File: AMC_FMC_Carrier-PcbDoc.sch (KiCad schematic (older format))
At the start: 19 parts

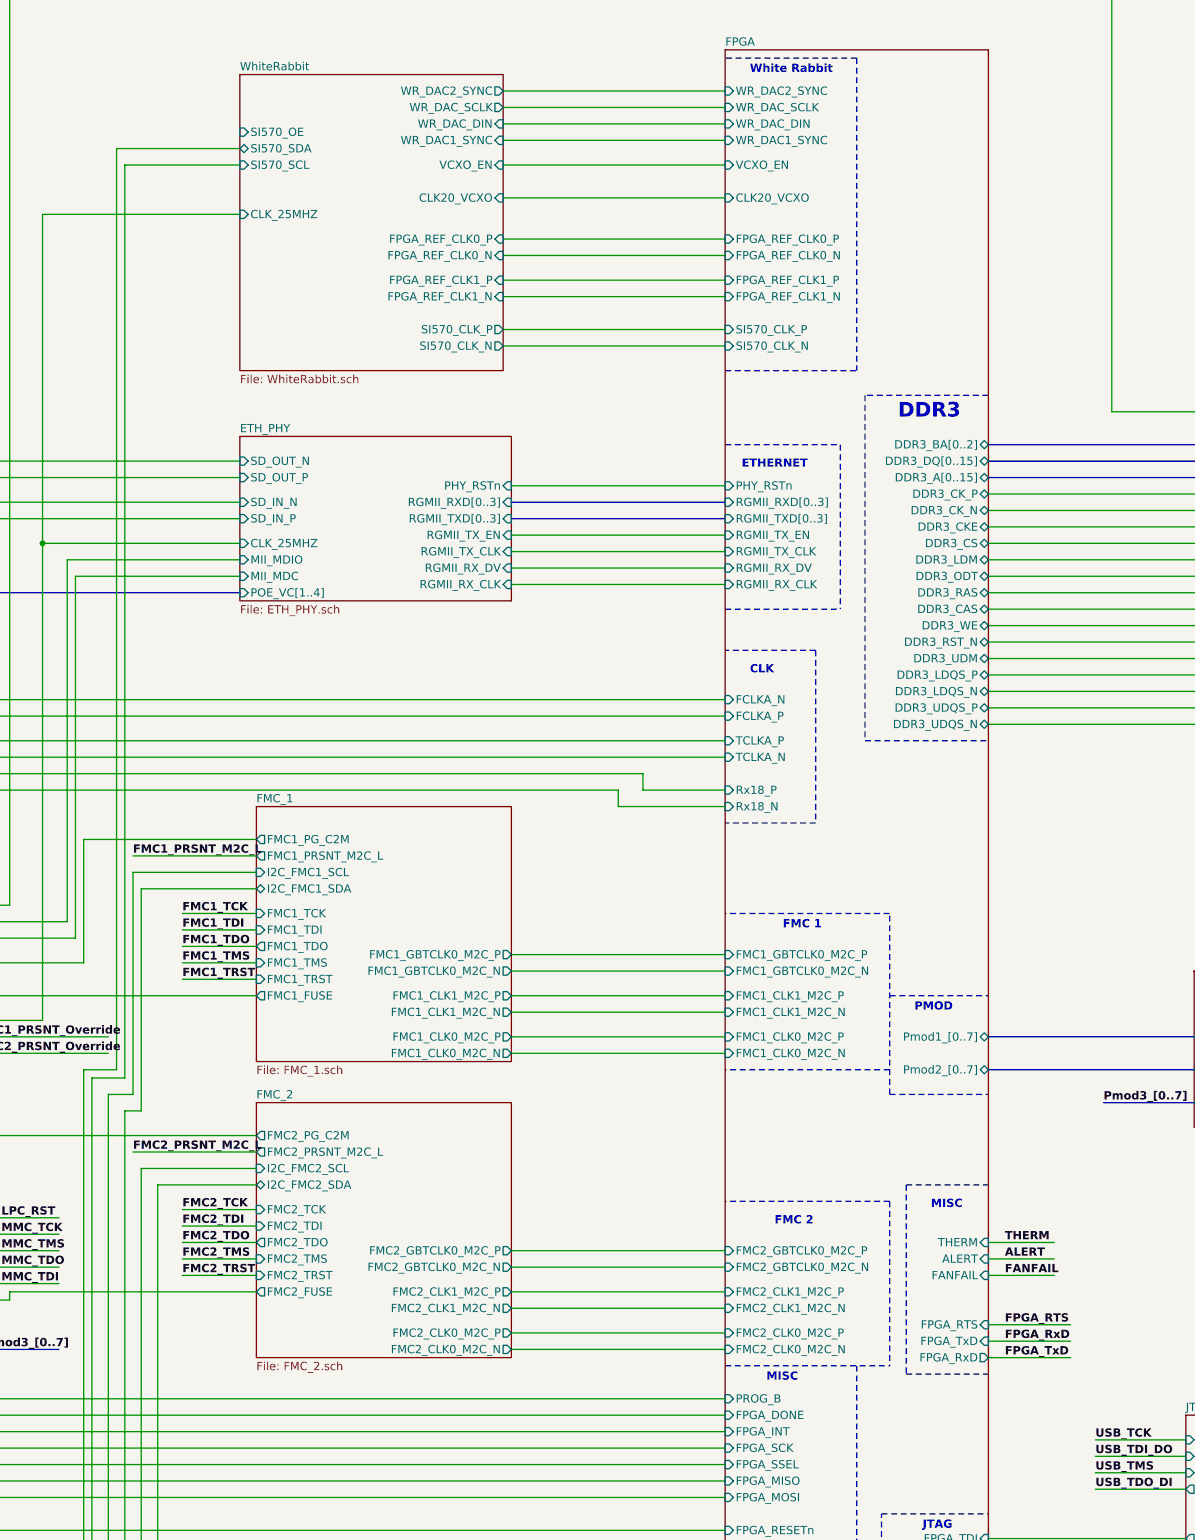
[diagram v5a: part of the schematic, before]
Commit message: SCH: connect SI570_OE to U39 P0_0 (pin 1)
... also rotated 6 net labels to make the
little _not connected_ square disappear
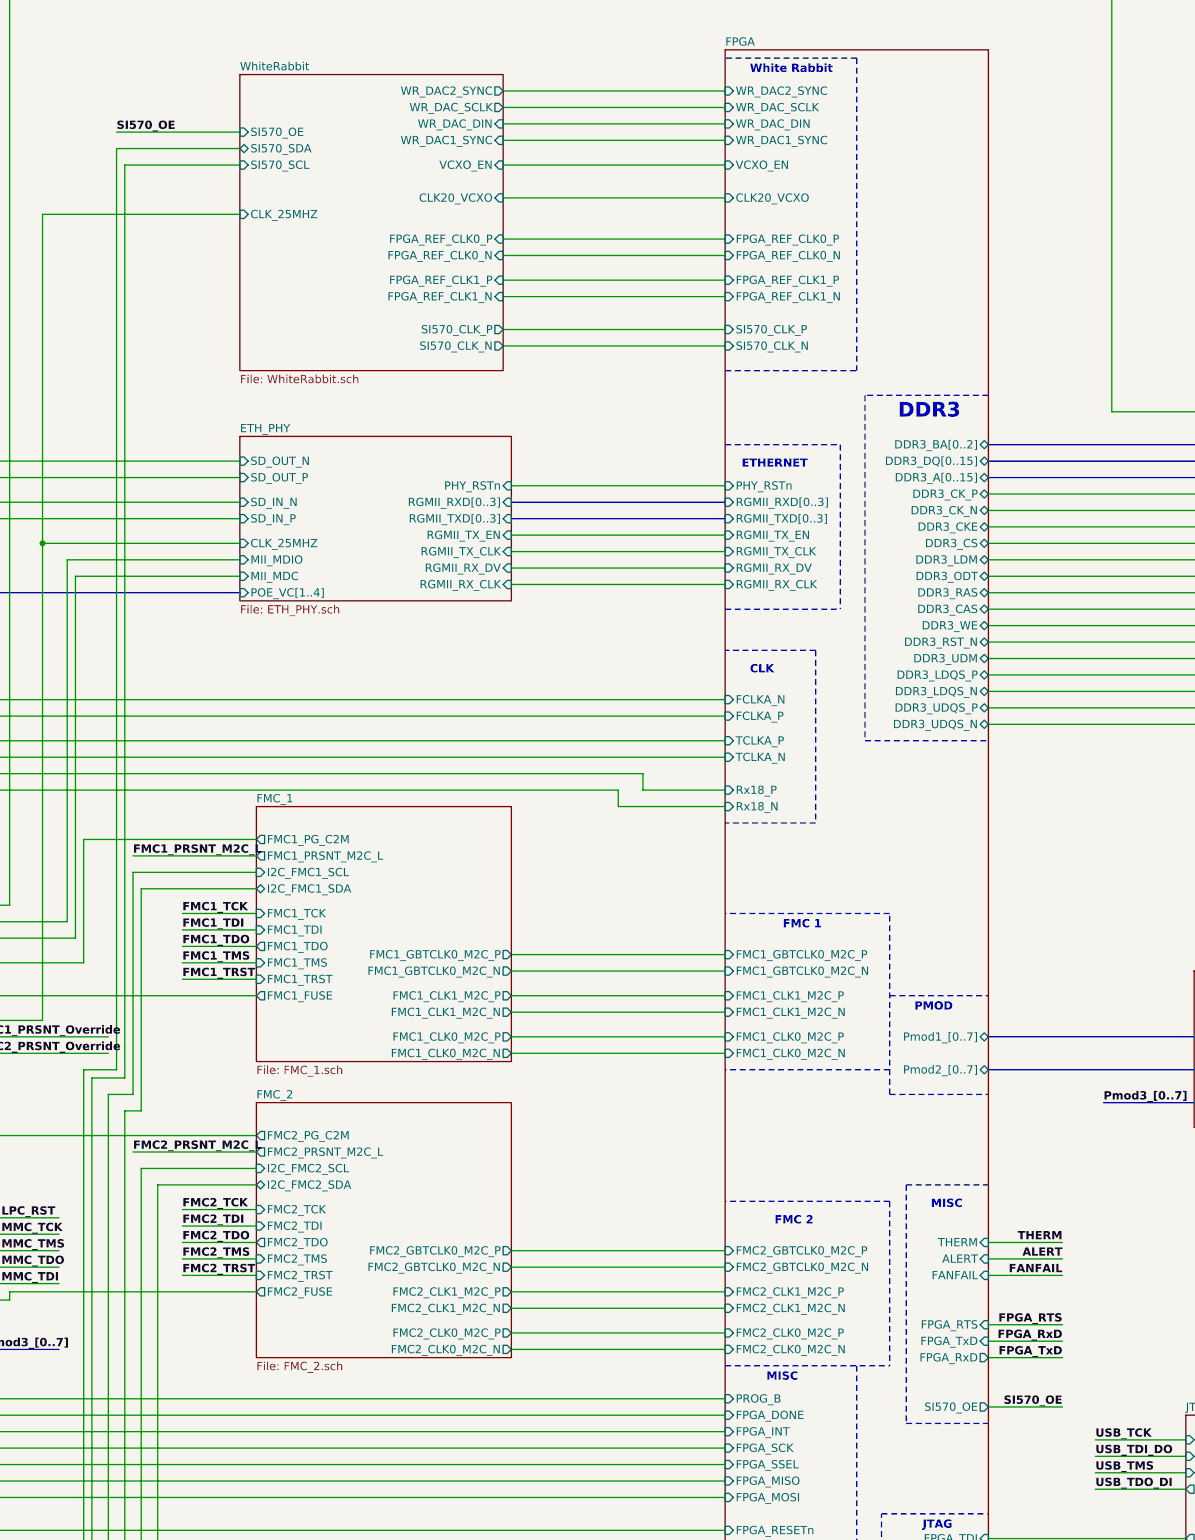
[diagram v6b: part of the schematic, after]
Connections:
- net labels added: SI570_OE
- wire segments 380 -> 382
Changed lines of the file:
@@
 F128 "SI570_CLK_P" I L 11350 3250 50
 F129 "SI570_CLK_N" I L 11350 3350 50
+F130 "SI570_OE" O R 12950 9800 50
 $EndSheet
 Wire Wire Line
@@
 Wire Wire Line
 	3500 10200 3100 10200
-Text Label 13050 8800 0    50   ~ 10
+Text Label 13400 8800 2    50   ~ 10
 THERM
-Text Label 13050 8900 0    50   ~ 10
+Text Label 13400 8900 2    50   ~ 10
 ALERT
-Text Label 13050 9000 0    50   ~ 10
+Text Label 13400 9000 2    50   ~ 10
 FANFAIL
 Wire Wire Line
-	13350 8800 12950 8800
-Wire Wire Line
-	13350 8900 12950 8900
-Wire Wire Line
-	13350 9000 12950 9000
+	13400 8800 12950 8800
+Wire Wire Line
+	13400 8900 12950 8900
+Wire Wire Line
+	13400 9000 12950 9000
 Wire Wire Line
 	6800 9750 11350 9750
@@
 Wire Bus Line
 	13650 7950 14200 7950
-Text Label 13050 9300 0    50   ~ 10
+Text Label 13400 9300 2    50   ~ 10
 FPGA_RTS
-Text Label 13050 9400 0    50   ~ 10
+Text Label 13400 9400 2    50   ~ 10
 FPGA_RxD
-Text Label 13050 9500 0    50   ~ 10
+Text Label 13400 9500 2    50   ~ 10
 FPGA_TxD
 Wire Wire Line
-	13450 9300 12950 9300
-Wire Wire Line
-	13450 9400 12950 9400
-Wire Wire Line
-	13450 9500 12950 9500
+	13400 9300 12950 9300
+Wire Wire Line
+	13400 9400 12950 9400
+Wire Wire Line
+	13400 9500 12950 9500
 Text Label 3550 8700 0    50   ~ 10
 FPGA_RTS
@@
 	12350 8550 12350 9550
 Wire Notes Line
-	12450 8450 12450 9600
-Wire Notes Line
-	12450 9600 12950 9600
+	12450 8450 12450 9900
+Wire Notes Line
+	12450 9900 12950 9900
 Wire Notes Line
 	12450 8450 12950 8450
@@
 Wire Wire Line
 	7450 7750 7650 7750
+Text Label 7650 2050 0    50   ~ 10
+SI570_OE
+Wire Wire Line
+	7650 2050 8400 2050
+Text Label 13400 9800 2    50   ~ 10
+SI570_OE
+Wire Wire Line
+	12950 9800 13400 9800
 $EndSCHEMATC

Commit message: Mounting holes
Add B13 near front panel
Un-ground B9 and B10, AMC features
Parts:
- added B13: PLATED_HOLE2.7_PAD5.0, Marble:HOLE2.7_PAD5.0, symbol Pads:PLATED_HOLE2.7_PAD5.0
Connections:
- wire segments 382 -> 381
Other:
- note added: "AMC holes not grounded"
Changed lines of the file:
@@
 L power:GND #PWR?
 U 1 1 5D64BA99
-P 3600 15250
+P 3450 15250
 AR Path="/5BD32060/5D64BA99" Ref="#PWR?"  Part="1"
 AR Path="/5BABAC65/5D64BA99" Ref="#PWR?"  Part="1"
@@
 AR Path="/5BCEDA3D/5D64BA99" Ref="#PWR?"  Part="1"
 AR Path="/5D64BA99" Ref="#PWR0266"  Part="1"
-F 0 "#PWR0266" H 3600 15000 50  0001 C CNN
-F 1 "GND" H 3605 15077 50  0000 C CNN
-F 2 "" H 3600 15250 50  0001 C CNN
-F 3 "" H 3600 15250 50  0001 C CNN
-	1    3600 15250
+F 0 "#PWR0266" H 3450 15000 50  0001 C CNN
+F 1 "GND" H 3455 15077 50  0000 C CNN
+F 2 "" H 3450 15250 50  0001 C CNN
+F 3 "" H 3450 15250 50  0001 C CNN
+	1    3450 15250
 	1    0    0    -1
 $EndComp
@@
 L power:GND #PWR?
 U 1 1 5D67B2EB
-P 3600 15500
+P 3450 15500
 AR Path="/5BD32060/5D67B2EB" Ref="#PWR?"  Part="1"
 AR Path="/5BABAC65/5D67B2EB" Ref="#PWR?"  Part="1"
@@
 AR Path="/5BCEDA3D/5D67B2EB" Ref="#PWR?"  Part="1"
 AR Path="/5D67B2EB" Ref="#PWR0467"  Part="1"
-F 0 "#PWR0467" H 3600 15250 50  0001 C CNN
-F 1 "GND" H 3605 15327 50  0000 C CNN
-F 2 "" H 3600 15500 50  0001 C CNN
-F 3 "" H 3600 15500 50  0001 C CNN
-	1    3600 15500
+F 0 "#PWR0467" H 3450 15250 50  0001 C CNN
+F 1 "GND" H 3455 15327 50  0000 C CNN
+F 2 "" H 3450 15500 50  0001 C CNN
+F 3 "" H 3450 15500 50  0001 C CNN
+	1    3450 15500
 	1    0    0    -1
 $EndComp
@@
 L Pads:PLATED_HOLE2.8_PAD0 B10
 U 1 1 5EBE33C9
-P 3400 15500
-F 0 "B10" H 3390 15605 50  0000 C CNN
-F 1 "PLATED_HOLE2.8_PAD0" H 3400 15345 50  0001 L CNN
-F 2 "Marble:HOLE2.8_PAD0" H 3400 15270 50  0001 L CNN
-F 3 "" H 3400 15195 50  0001 L CNN
-F 4 "This work is licensed under the Creative Commons CC-BY-SA 4.0 License. To the extent that circuit schematics that use Licensed Material can be considered to be ‘Adapted Material’, then the copyright holder waives article 3.b of the license with respect to these schematics." H 3400 12495 50  0001 L CNN "License"
-F 5 "dnf" H 3400 15500 50  0001 C CNN "config"
-	1    3400 15500
+P 5000 15500
+F 0 "B10" H 4990 15605 50  0000 C CNN
+F 1 "PLATED_HOLE2.8_PAD0" H 5000 15345 50  0001 L CNN
+F 2 "Marble:HOLE2.8_PAD0" H 5000 15270 50  0001 L CNN
+F 3 "" H 5000 15195 50  0001 L CNN
+F 4 "This work is licensed under the Creative Commons CC-BY-SA 4.0 License. To the extent that circuit schematics that use Licensed Material can be considered to be ‘Adapted Material’, then the copyright holder waives article 3.b of the license with respect to these schematics." H 5000 12495 50  0001 L CNN "License"
+F 5 "dnf" H 5000 15500 50  0001 C CNN "config"
+	1    5000 15500
 	1    0    0    -1
 $EndComp
@@
 L Pads:SLOT_2_11 B9
 U 1 1 5EBE3B57
-P 3400 15250
-F 0 "B9" H 3400 15350 50  0000 C CNN
-F 1 "SLOT_2_11" H 3400 15095 50  0001 L CNN
-F 2 "Marble:HOLE2_SLOT11" H 3400 15020 50  0001 L CNN
-F 3 "" H 3400 14945 50  0001 L CNN
-F 4 "This work is licensed under the Creative Commons CC-BY-SA 4.0 License. To the extent that circuit schematics that use Licensed Material can be considered to be ‘Adapted Material’, then the copyright holder waives article 3.b of the license with respect to these schematics." H 3400 12245 50  0001 L CNN "License"
-F 5 "dnf" H 3400 15250 50  0001 C CNN "config"
-	1    3400 15250
-	1    0    0    -1
-$EndComp
-Wire Wire Line
-	3400 15250 3600 15250
-Wire Wire Line
-	3400 15250 3250 15250
-Connection ~ 3400 15250
+P 5000 15250
+F 0 "B9" H 5000 15350 50  0000 C CNN
+F 1 "SLOT_2_11" H 5000 15095 50  0001 L CNN
+F 2 "Marble:HOLE2_SLOT11" H 5000 15020 50  0001 L CNN
+F 3 "" H 5000 14945 50  0001 L CNN
+F 4 "This work is licensed under the Creative Commons CC-BY-SA 4.0 License. To the extent that circuit schematics that use Licensed Material can be considered to be ‘Adapted Material’, then the copyright holder waives article 3.b of the license with respect to these schematics." H 5000 12245 50  0001 L CNN "License"
+F 5 "dnf" H 5000 15250 50  0001 C CNN "config"
+	1    5000 15250
+	1    0    0    -1
+$EndComp
 Connection ~ 3250 15250
-Wire Wire Line
-	3250 15500 3400 15500
 Connection ~ 3250 15500
-Wire Wire Line
-	3400 15500 3600 15500
-Connection ~ 3400 15500
 $Comp
 L Pads:PLATED_HOLE2.7_PAD5.0 B11
@@
 L power:GND #PWR?
 U 1 1 5ECDA445
-P 4350 15250
+P 4500 15250
 AR Path="/5BD32060/5ECDA445" Ref="#PWR?"  Part="1"
 AR Path="/5BABAC65/5ECDA445" Ref="#PWR?"  Part="1"
@@
 AR Path="/5BCEDA3D/5ECDA445" Ref="#PWR?"  Part="1"
 AR Path="/5ECDA445" Ref="#PWR0680"  Part="1"
-F 0 "#PWR0680" H 4350 15000 50  0001 C CNN
-F 1 "GND" H 4355 15077 50  0000 C CNN
-F 2 "" H 4350 15250 50  0001 C CNN
-F 3 "" H 4350 15250 50  0001 C CNN
-	1    4350 15250
+F 0 "#PWR0680" H 4500 15000 50  0001 C CNN
+F 1 "GND" H 4505 15077 50  0000 C CNN
+F 2 "" H 4500 15250 50  0001 C CNN
+F 3 "" H 4500 15250 50  0001 C CNN
+	1    4500 15250
 	1    0    0    -1
 $EndComp
@@
 	4000 15250 4150 15250
 Wire Wire Line
-	4150 15250 4350 15250
+	4150 15250 4300 15250
 Connection ~ 4150 15250
 Wire Notes Line
@@
 Wire Wire Line
 	12950 9800 13400 9800
+Wire Wire Line
+	3250 15500 3450 15500
+Wire Wire Line
+	3250 15250 3450 15250
+$Comp
+L Pads:PLATED_HOLE2.7_PAD5.0 B13
+U 1 1 5F05A5A0
+P 4300 15250
+F 0 "B13" H 4285 15355 50  0000 C CNN
+F 1 "PLATED_HOLE2.7_PAD5.0" H 4300 15080 60  0001 L CNN
+F 2 "Marble:HOLE2.7_PAD5.0" H 4300 14270 60  0001 L CNN
+F 3 "" H 4300 14900 60  0001 L CNN
+F 4 "Plated Hole" H 4300 14810 60  0001 L CNN "Pole4"
+F 5 "PLATED_HOLE2.7_PAD5.0" H 4300 14810 60  0001 L CNN "Part Number"
+F 6 "Single Terminal Socket" H 4300 14720 60  0001 L CNN "Library Ref"
+F 7 "SchLib\\Pads.SchLib" H 4300 14630 60  0001 L CNN "Library Path"
+F 8 " " H 4300 14540 60  0001 L CNN "Comment"
+F 9 "Standard (No BOM)" H 4300 14450 60  0001 L CNN "Component Kind"
+F 10 "Standard (No BOM)" H 4300 14360 60  0001 L CNN "Component Type"
+F 11 "1" H 4300 14180 60  0001 L CNN "Pin Count"
+F 12 " " H 4300 14090 60  0001 L CNN "Case"
+F 13 "PcbLib\\Pads.PcbLib" H 4300 14000 60  0001 L CNN "Footprint Path"
+F 14 "MTG270_500" H 4300 13910 60  0001 L CNN "Footprint Ref"
+F 15 "Plated Hole" H 4300 13820 60  0001 L CNN "Family"
+F 16 "No" H 4300 13730 60  0001 L CNN "Mounted"
+F 17 "No" H 4300 13640 60  0001 L CNN "Socket"
+F 18 "No" H 4300 13550 60  0001 L CNN "SMD"
+F 19 "No" H 4300 13460 60  0001 L CNN "Sense"
+F 20 " " H 4300 13370 60  0001 L CNN "Sense Comment"
+F 21 "None" H 4300 13280 60  0001 L CNN "Status"
+F 22 " " H 4300 13190 60  0001 L CNN "Status Comment"
+F 23 "Plated Through Hole: Hole Dia.=2.7mm Pad Dia.=5.0mm" H 4300 13010 60  0001 L CNN "Part Description"
+F 24 " " H 4300 12920 60  0001 L CNN "Manufacturer"
+F 25 " " H 4300 12830 60  0001 L CNN "Manufacturer Part Number"
+F 26 "0mm" H 4300 12740 60  0001 L CNN "ComponentHeight"
+F 27 " " H 4300 12650 60  0001 L CNN "Manufacturer1 Example"
+F 28 " " H 4300 12560 60  0001 L CNN "Manufacturer1 Part Number"
+F 29 " " H 4300 12470 60  0001 L CNN "Manufacturer1 ComponentHeight"
+F 30 " " H 4300 12200 60  0001 L CNN "ComponentLink1Description"
+F 31 " " H 4300 12020 60  0001 L CNN "ComponentLink2Description"
+F 32 "CERN DEM JMW" H 4300 11930 60  0001 L CNN "Author"
+F 33 "09/27/11 00:00:00" H 4300 11840 60  0001 L CNN "CreateDate"
+F 34 "09/27/11 00:00:00" H 4300 11750 60  0001 L CNN "LatestRevisionDate"
+F 35 "Plated Through Hole: Hole Dia.=2.7mm Pad Dia.=5.0mm" H 4300 11660 60  0001 L CNN "PackageDescription"
+F 36 "Eletro-mechanical.DbLib" H 4300 11570 60  0001 L CNN "Library Name"
+F 37 "This work is licensed under the Creative Commons CC-BY-SA 4.0 License. To the extent that circuit schematics that use Licensed Material can be considered to be ‘Adapted Material’, then the copyright holder waives article 3.b of the license with respect to these schematics." H 4300 11480 60  0001 L CNN "License"
+F 38 "dnf" H 4300 15250 50  0001 C CNN "config"
+	1    4300 15250
+	1    0    0    -1
+$EndComp
+Connection ~ 4300 15250
+Wire Wire Line
+	4300 15250 4500 15250
+Text Notes 4950 15050 0    50   ~ 0
+AMC holes not grounded
 $EndSCHEMATC

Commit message: Start adding isolation for I2C_FPGA_SW_RST and EXP_INT
Adds U47, another TCA9517
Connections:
- wire segments 381 -> 383
- no-connect marks 1 -> 3
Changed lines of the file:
@@
 Text Notes 4950 15050 0    50   ~ 0
 AMC holes not grounded
+Wire Wire Line
+	5000 15250 5150 15250
+Wire Wire Line
+	5000 15500 5150 15500
+NoConn ~ 5150 15250
+NoConn ~ 5150 15500
 $EndSCHEMATC
